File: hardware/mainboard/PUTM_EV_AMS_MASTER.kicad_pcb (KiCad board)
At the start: 4 copper layers, 60 x 100 mm, 172 parts, among them IC3 BQ79600PWRQ1, IC6 AMC3330DWER, IC7 AMC3330DWER, IC8 ADC 24bit, IC9 LTC1799, J1 Conn_02x10_Odd_Even, J10 M300-MV10345M1, J2 XIAO ESP32S3 Sense, J3 Conn_02x04_Odd_Even, J4 FTSH-107-01-L-D-K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

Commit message: minifix2
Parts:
- moved C101 2.98 mm to (129.3, 126.7)
- moved C102 2.98 mm to (130.8, 126.7)
- moved C103 2.98 mm to (123.4, 126.7)
- moved C104 2.98 mm to (124.9, 126.7)
- moved C105 2.98 mm to (124.9, 119.5)
- moved R21 2.98 mm to (122.0, 126.7)
- moved R25 2.98 mm to (126.4, 126.7)
- moved R26 2.98 mm to (126.4, 119.5)
- moved R17 2.98 mm to (127.8, 126.7)
- moved R20 2.98 mm to (132.2, 126.7)
- moved D25 2.98 mm to (124.2, 123.1)
- moved D26 2.98 mm to (130.0, 123.1)
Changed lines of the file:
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@@
 	(footprint "Capacitor_SMD:C_0603_1608Metric"
 		(layer "F.Cu")
-		(at 124.5125 123.7 90)
+		(at 124.9 126.65 90)
 		(descr "Capacitor SMD 0603 (1608 Metric), square (rectangular) end terminal, IPC_7351 nominal, (Body size source: IPC-SM-782 page 76, https://www.pcb-3d.com/wordpress/wp-content/uploads/ipc-sm-782a_amendment_1_and_2.pdf), generated with kicad-footprint-generator")
 		(tags "capacitor")
@@
 	(footprint "Package_TO_SOT_SMD:SOT-23-6"
 		(layer "F.Cu")
-		(at 129.65 120.15 90)
+		(at 130.0375 123.1 90)
 		(descr "SOT, 6 Pin (JEDEC MO-178 Var AB https://www.jedec.org/document_search?search_api_views_fulltext=MO-178), generated with kicad-footprint-generator ipc_gullwing_generator.py")
 		(tags "SOT TO_SOT_SMD")
@@
 	(footprint "Resistor_SMD:R_0603_1608Metric"
 		(layer "F.Cu")
-		(at 131.8625 123.7 -90)
+		(at 132.25 126.65 -90)
 		(descr "Resistor SMD 0603 (1608 Metric), square (rectangular) end terminal, IPC_7351 nominal, (Body size source: IPC-SM-782 page 72, https://www.pcb-3d.com/wordpress/wp-content/uploads/ipc-sm-782a_amendment_1_and_2.pdf), generated with kicad-footprint-generator")
 		(tags "resistor")
@@
 	(footprint "Capacitor_SMD:C_0603_1608Metric"
 		(layer "F.Cu")
-		(at 124.5375 116.6 -90)
+		(at 124.925 119.55 -90)
 		(descr "Capacitor SMD 0603 (1608 Metric), square (rectangular) end terminal, IPC_7351 nominal, (Body size source: IPC-SM-782 page 76, https://www.pcb-3d.com/wordpress/wp-content/uploads/ipc-sm-782a_amendment_1_and_2.pdf), generated with kicad-footprint-generator")
 		(tags "capacitor")
@@
 	(footprint "Capacitor_SMD:C_0603_1608Metric"
 		(layer "F.Cu")
-		(at 123.0375 123.7 90)
+		(at 123.425 126.65 90)
 		(descr "Capacitor SMD 0603 (1608 Metric), square (rectangular) end terminal, IPC_7351 nominal, (Body size source: IPC-SM-782 page 76, https://www.pcb-3d.com/wordpress/wp-content/uploads/ipc-sm-782a_amendment_1_and_2.pdf), generated with kicad-footprint-generator")
 		(tags "capacitor")
@@
 	(footprint "Package_TO_SOT_SMD:SOT-23-6"
 		(layer "F.Cu")
-		(at 123.775 120.15 90)
+		(at 124.1625 123.1 90)
 		(descr "SOT, 6 Pin (JEDEC MO-178 Var AB https://www.jedec.org/document_search?search_api_views_fulltext=MO-178), generated with kicad-footprint-generator ipc_gullwing_generator.py")
 		(tags "SOT TO_SOT_SMD")
@@
 	(footprint "Resistor_SMD:R_0603_1608Metric"
 		(layer "F.Cu")
-		(at 121.5625 123.7 -90)
+		(at 121.95 126.65 -90)
 		(descr "Resistor SMD 0603 (1608 Metric), square (rectangular) end terminal, IPC_7351 nominal, (Body size source: IPC-SM-782 page 72, https://www.pcb-3d.com/wordpress/wp-content/uploads/ipc-sm-782a_amendment_1_and_2.pdf), generated with kicad-footprint-generator")
 		(tags "resistor")
@@
 	(footprint "Resistor_SMD:R_0603_1608Metric"
 		(layer "F.Cu")
-		(at 126.0125 116.6 90)
+		(at 126.4 119.55 90)
 		(descr "Resistor SMD 0603 (1608 Metric), square (rectangular) end terminal, IPC_7351 nominal, (Body size source: IPC-SM-782 page 72, https://www.pcb-3d.com/wordpress/wp-content/uploads/ipc-sm-782a_amendment_1_and_2.pdf), generated with kicad-footprint-generator")
 		(tags "resistor")
@@
 	(footprint "Capacitor_SMD:C_0603_1608Metric"
 		(layer "F.Cu")
-		(at 130.3875 123.7 90)
+		(at 130.775 126.65 90)
 		(descr "Capacitor SMD 0603 (1608 Metric), square (rectangular) end terminal, IPC_7351 nominal, (Body size source: IPC-SM-782 page 76, https://www.pcb-3d.com/wordpress/wp-content/uploads/ipc-sm-782a_amendment_1_and_2.pdf), generated with kicad-footprint-generator")
 		(tags "capacitor")
@@
 	(footprint "Capacitor_SMD:C_0603_1608Metric"
 		(layer "F.Cu")
-		(at 128.9125 123.7 90)
+		(at 129.3 126.65 90)
 		(descr "Capacitor SMD 0603 (1608 Metric), square (rectangular) end terminal, IPC_7351 nominal, (Body size source: IPC-SM-782 page 76, https://www.pcb-3d.com/wordpress/wp-content/uploads/ipc-sm-782a_amendment_1_and_2.pdf), generated with kicad-footprint-generator")
 		(tags "capacitor")
@@
 	(footprint "Resistor_SMD:R_0603_1608Metric"
 		(layer "F.Cu")
-		(at 125.9875 123.7 -90)
+		(at 126.375 126.65 -90)
 		(descr "Resistor SMD 0603 (1608 Metric), square (rectangular) end terminal, IPC_7351 nominal, (Body size source: IPC-SM-782 page 72, https://www.pcb-3d.com/wordpress/wp-content/uploads/ipc-sm-782a_amendment_1_and_2.pdf), generated with kicad-footprint-generator")
 		(tags "resistor")
@@
 	(footprint "Resistor_SMD:R_0603_1608Metric"
 		(layer "F.Cu")
-		(at 127.4625 123.7 -90)
+		(at 127.85 126.65 -90)
 		(descr "Resistor SMD 0603 (1608 Metric), square (rectangular) end terminal, IPC_7351 nominal, (Body size source: IPC-SM-782 page 72, https://www.pcb-3d.com/wordpress/wp-content/uploads/ipc-sm-782a_amendment_1_and_2.pdf), generated with kicad-footprint-generator")
 		(tags "resistor")
@@
 	)
 	(gr_rect
-		(start 120.6875 114.975)
-		(end 132.7375 125.325)
+		(start 121.075 117.925)
+		(end 133.125 128.275)
 		(stroke
 			(width 0.2)
@@
 	)
 	(gr_rect
-		(start 120.6875 125.325)
-		(end 126.7875 127.325)
+		(start 121.075 128.275)
+		(end 127.175 130.275)
 		(stroke
 			(width 0.2)
@@
 	)
 	(gr_text "INPUTS"
-		(at 123.7125 126.275 180)
+		(at 124.1 129.225 180)
 		(layer "F.SilkS" knockout)
 		(effects
@@
 	)
 	(segment
-		(start 124.5125 122.925)
-		(end 125.9375 122.925)
+		(start 124.9 125.875)
+		(end 126.325 125.875)
 		(width 0.25)
 		(layer "F.Cu")
@@
 	)
 	(segment
-		(start 124.5125 122.925)
-		(end 124.5125 121.5)
+		(start 124.9 125.875)
+		(end 124.9 124.45)
 		(width 0.25)
 		(layer "F.Cu")
@@
 	)
 	(segment
-		(start 124.5125 121.5)
-		(end 124.725 121.2875)
+		(start 124.9 124.45)
+		(end 125.1125 124.2375)
 		(width 0.25)
 		(layer "F.Cu")
@@
 	)
 	(segment
-		(start 128.8625 122.875)
-		(end 128.9125 122.925)
+		(start 129.25 125.825)
+		(end 129.3 125.875)
 		(width 0.25)
 		(layer "F.Cu")
@@
 	)
 	(segment
-		(start 127.4625 122.875)
-		(end 128.8625 122.875)
+		(start 127.85 125.825)
+		(end 129.25 125.825)
 		(width 0.25)
 		(layer "F.Cu")
@@
 	)
 	(segment
-		(start 128.9125 122.925)
-		(end 128.9125 121.5)
+		(start 129.3 125.875)
+		(end 129.3 124.45)
 		(width 0.25)
 		(layer "F.Cu")
@@
 	)
 	(segment
-		(start 128.9125 121.5)
-		(end 128.7 121.2875)
+		(start 129.3 124.45)
+		(end 129.0875 124.2375)
 		(width 0.25)
 		(layer "F.Cu")
@@
 	)
 	(segment
-		(start 130.3875 121.5)
-		(end 130.6 121.2875)
+		(start 130.775 124.45)
+		(end 130.9875 124.2375)
 		(width 0.25)
 		(layer "F.Cu")
@@
 	)
 	(segment
-		(start 130.3875 122.925)
-		(end 131.8125 122.925)
+		(start 130.775 125.875)
+		(end 132.2 125.875)
 		(width 0.25)
 		(layer "F.Cu")
@@
 	)
 	(segment
-		(start 130.3875 122.925)
-		(end 130.3875 121.5)
+		(start 130.775 125.875)
+		(end 130.775 124.45)
 		(width 0.25)
 		(layer "F.Cu")
@@
 	)
 	(segment
-		(start 131.8125 122.925)
-		(end 131.8625 122.875)
+		(start 132.2 125.875)
+		(end 132.25 125.825)
 		(width 0.25)
 		(layer "F.Cu")
@@
 	)
 	(segment
-		(start 131.8625 124.375)
-		(end 131.9125 124.325)
+		(start 132.25 127.325)
+		(end 132.3 127.275)
 		(width 0.1275)
 		(layer "F.Cu")
@@
 	)
 	(segment
-		(start 124.5375 117.375)
-		(end 124.5375 118.825)
+		(start 124.925 120.325)
+		(end 124.925 121.775)
 		(width 0.25)
 		(layer "F.Cu")
@@
 	)
 	(segment
-		(start 124.5375 117.375)
-		(end 125.9625 117.375)
+		(start 124.925 120.325)
+		(end 126.35 120.325)
 		(width 0.25)
 		(layer "F.Cu")
@@
 	)
 	(segment
-		(start 124.5375 118.825)
-		(end 124.725 119.0125)
+		(start 124.925 121.775)
+		(end 125.1125 121.9625)
 		(width 0.25)
 		(layer "F.Cu")
@@
 	)
 	(segment
-		(start 123.0375 122.925)
-		(end 123.0375 121.5)
+		(start 123.425 125.875)
+		(end 123.425 124.45)
 		(width 0.25)
 		(layer "F.Cu")
@@
 	)
 	(segment
-		(start 123.0375 122.925)
-		(end 121.6125 122.925)
+		(start 123.425 125.875)
+		(end 122 125.875)
 		(width 0.25)
 		(layer "F.Cu")
@@
 	)
 	(segment
-		(start 123.0375 121.5)
-		(end 122.825 121.2875)
+		(start 123.425 124.45)
+		(end 123.2125 124.2375)
 		(width 0.25)
 		(layer "F.Cu")
@@
 	)
 	(segment
-		(start 127.5625 124.375)
-		(end 127.5125 124.325)
+		(start 127.95 127.325)
+		(end 127.9 127.275)
 		(width 0.1275)
 		(layer "F.Cu")
@@
 		(polygon
 			(pts
-				(xy 126.7875 127.325) (xy 126.7875 125.325) (xy 120.6875 125.325) (xy 120.6875 127.325)
+				(xy 127.175 130.275) (xy 127.175 128.275) (xy 121.075 128.275) (xy 121.075 130.275)
 			)
 		)

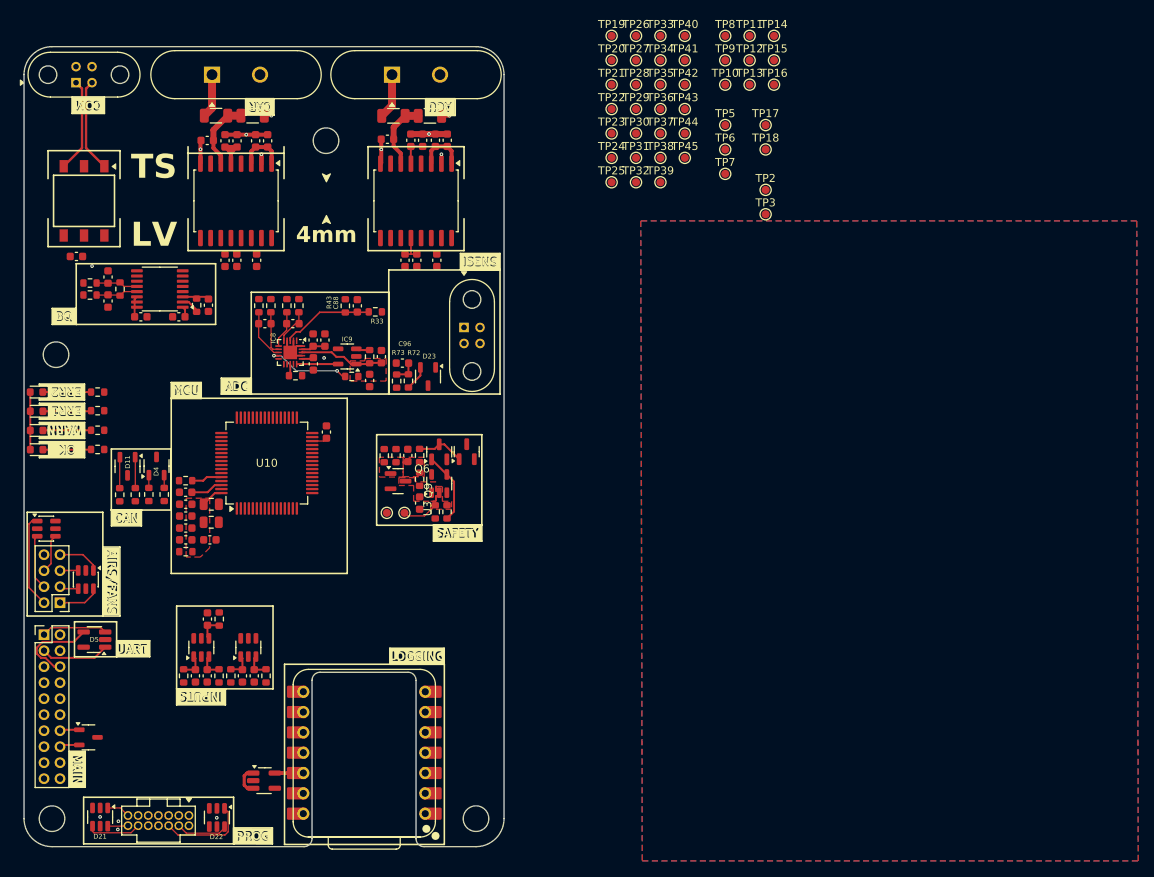
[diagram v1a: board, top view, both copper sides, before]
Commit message: Plytka chyba fajnie zrobiona oprocz teardropow bo kicad 10 jest dziwny
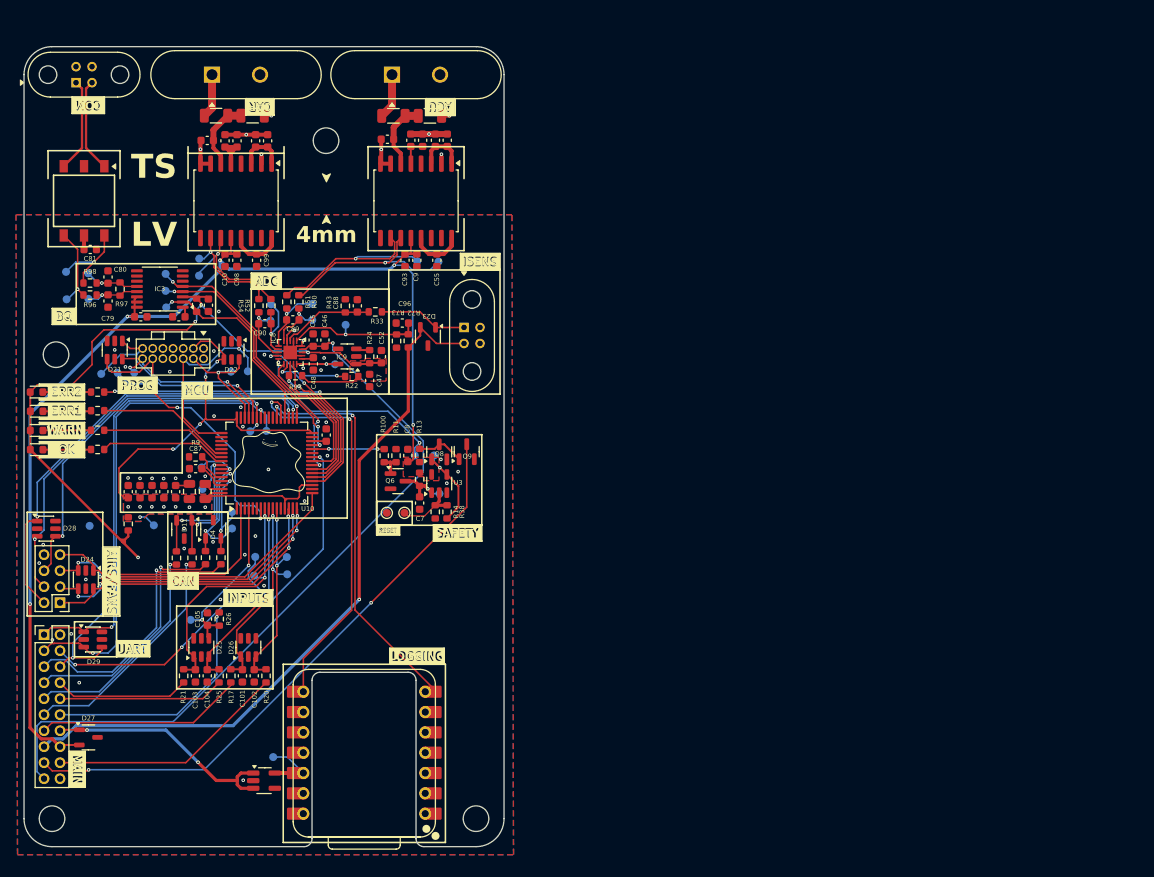
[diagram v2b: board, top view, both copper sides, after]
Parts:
- removed D5: ESDS304, Package_TO_SOT_SMD:SOT-23-5_HandSoldering
- removed TP11, TP19, TP20, TP21, TP22, TP23, TP24, TP25, TP26, TP27, TP28, TP29, TP30, TP35, TP36, TP37, TP38, TP39, TP40, TP41, TP42, TP9: TestPoint_Small, TestPoint:TestPoint_Pad_D1.0mm
- added ACU_OUT+1: ACU_OUT+, TestPoint:TestPoint_Pad_D1.0mm, B.Cu at (153.8, 74.9)
- added ACU_OUT-1: ACU_OUT-, TestPoint:TestPoint_Pad_D1.0mm, B.Cu at (151.2, 74.8)
- added CAR_OUT+1: CAR_OUT+, TestPoint:TestPoint_Pad_D1.0mm, B.Cu at (123.9, 76.6)
- added CAR_OUT-1: CAR_OUT-, TestPoint:TestPoint_Pad_D1.0mm, B.Cu at (123.9, 74.5)
- added D29: 3.6V/400W, Package_TO_SOT_SMD:SOT-23-6, F.Cu at (110.6, 122.1)
- added G***: LOGO, LOGO, F.Cu at (132.5, 99.7)
- added ISO_SPI_OUT+1: ISO_SPI_OUT+, TestPoint:TestPoint_Pad_D1.0mm, B.Cu at (107.3, 79.6)
- added ISO_SPI_OUT-1: ISO_SPI_OUT-, TestPoint:TestPoint_Pad_D1.0mm, B.Cu at (107.2, 76.2)
- added RX1: TestPoint_Small, TestPoint:TestPoint_Pad_D1.0mm, B.Cu at (132.3, 96.0)
- added SWDIO1: SWDIO, TestPoint:TestPoint_Pad_D1.0mm, B.Cu at (127.9, 88.6)
- added TX1: TestPoint_Small, TestPoint:TestPoint_Pad_D1.0mm, B.Cu at (130.3, 96.1)
- added UC_AIR_AUX_M1: TestPoint_Small, TestPoint:TestPoint_Pad_D1.0mm, B.Cu at (134.9, 114.0)
- added UC_AIR_AUX_P1: TestPoint_Small, TestPoint:TestPoint_Pad_D1.0mm, B.Cu at (122.8, 119.7)
- added UC_AIR_AUX_PRE1: TestPoint_Small, TestPoint:TestPoint_Pad_D1.0mm, B.Cu at (130.8, 114.1)
- added UC_CANFD1_RX1: TestPoint_Small, TestPoint:TestPoint_Pad_D1.0mm, B.Cu at (128.0, 108.2)
- added UC_CANFD1_TX1: TestPoint_Small, TestPoint:TestPoint_Pad_D1.0mm, B.Cu at (128.0, 106.2)
- added UC_CANFD1_TX2: TestPoint_Small, TestPoint:TestPoint_Pad_D1.0mm, B.Cu at (124.3, 103.3)
- added UC_CANFD2_RX1: TestPoint_Small, TestPoint:TestPoint_Pad_D1.0mm, B.Cu at (124.2, 100.6)
- added UC_IN1: TestPoint_Small, TestPoint:TestPoint_Pad_D1.0mm, B.Cu at (134.8, 111.8)
- added UC_IN2: TestPoint_Small, TestPoint:TestPoint_Pad_D1.0mm, B.Cu at (130.9, 111.8)
- TP10: value TestPoint_Small -> GND; moved to B.Cu
- TP12: value TestPoint_Small -> ACU_V+; moved to B.Cu
- TP13: value TestPoint_Small -> ACU_V-; moved to B.Cu
- TP14: value TestPoint_Small -> CAR_V+; moved to B.Cu
- TP15: value TestPoint_Small -> CAR_V-; moved to B.Cu
- TP16: value TestPoint_Small -> 4MHz; moved to B.Cu
- TP17: value TestPoint_Small -> COMHP; moved to B.Cu
- TP18: value TestPoint_Small -> COMHN; moved to B.Cu
- TP2: value TestPoint_Small -> +3.3V_PROT; moved to B.Cu
- TP3: value TestPoint_Small -> +3.3VMCU; moved to B.Cu
- TP31: value TestPoint_Small -> DBG_RX; moved to B.Cu
- TP32: value TestPoint_Small -> DBG_TX; moved to B.Cu
- TP33: value TestPoint_Small -> NRST; moved to B.Cu
- TP34: value TestPoint_Small -> SWCLK; moved to B.Cu
- TP43: value TestPoint_Small -> SPI_TX; moved to B.Cu
- TP44: value TestPoint_Small -> SPI_RX; moved to B.Cu
- TP45: value TestPoint_Small -> FLT; moved to B.Cu
- TP5: value TestPoint_Small -> CAP_VOLT; moved to B.Cu
- TP6: value TestPoint_Small -> LATCHED_ERR; moved to B.Cu
- TP7: value TestPoint_Small -> WTDG_ERROR; moved to B.Cu
- TP8: value TestPoint_Small -> +5VA_MEAS; moved to B.Cu
- moved TP10 96.7 mm to (110.2, 107.9), turned to 180 degrees
- moved TP2 93.9 mm to (133.2, 136.8), turned to 180 degrees
- moved TP17 87.4 mm to (110.0, 79.5), turned to 180 degrees
- moved TP18 86.1 mm to (110.0, 76.3), turned to 180 degrees
- moved TP3 85.8 mm to (118.2, 107.8), turned to 180 degrees
- moved G*** 81.3 mm to (119.0, 133.5)
- moved TP33 79.9 mm to (113.7, 88.8), turned to 180 degrees
- moved TP31 72.1 mm to (111.7, 88.9), turned to 180 degrees
- moved TP14 71.3 mm to (132.9, 80.2), turned to 180 degrees
- moved TP15 70.9 mm to (132.8, 82.2), turned to 180 degrees
- moved TP43 68.8 mm to (119.7, 78.5), turned to 180 degrees
- moved TP45 67.5 mm to (119.8, 80.6), turned to 180 degrees
- moved TP44 67.2 mm to (119.7, 76.4), turned to 180 degrees
- moved TP32 67.1 mm to (115.8, 88.8), turned to 180 degrees
- moved TP16 65.1 mm to (140.9, 87.7), turned to 180 degrees
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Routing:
- net +5VIO: track 8.66 -> 141.7 mm, vias 0 -> 5
- net +3.3VIO: track 27.2 -> 149.0 mm, vias 0 -> 6
- net +3.3VA: track 3.03 -> 93.3 mm, vias 0 -> 1
- net +5VA: track 3.13 -> 90.5 mm, vias 0 -> 1
- net /ERROR_RELAY-: track 0.00 -> 74.8 mm, vias 0 -> 2
- net +3.3VMCU: track 2.80 -> 67.7 mm, vias 0 -> 12
- net /UART_RX: track 8.58 -> 61.9 mm, vias 0 -> 2
- net /DETVUSB: track 0.00 -> 52.3 mm, vias 0 -> 3
- net /MCU/LOG_UART_TX: track 0.00 -> 50.5 mm, vias 0 -> 2
- net /UART_TX: track 8.23 -> 58.5 mm, vias 0 -> 3
- net /MCU/LOG_UART_RX: track 0.00 -> 49.9 mm, vias 0 -> 2
- net /AIR_P-: track 6.90 -> 52.4 mm, vias 0 -> 2
- net /AMS_ERROR: track 5.94 -> 50.6 mm, vias 0 -> 2
- net /AIR_PRE-: track 11.8 -> 56.2 mm, vias 0 -> 2
- net /AIR_M-: track 4.89 -> 48.4 mm, vias 0 -> 2
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- added copper zone on B.Cu, net +3.3VMCU
- removed copper zone on F.Cu, net /Safety/CAP_VOLT
- removed copper zone on F.Cu, net /Safety/CT_G
- removed copper zone on F.Cu, net Net-(R14-Pad2)
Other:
- board text added: "RESET"
